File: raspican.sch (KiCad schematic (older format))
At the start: 3 parts, among them P1 CONN_13X2

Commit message: start wiring stuff up
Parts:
- added D1: LED, symbol LED
- added J2: CONN_01X06, symbol CONN_01X06
- added R10, R8, R9: 1KΩ, symbol R
- added R6: 18KΩ, symbol R
- added R7: 10KΩ, symbol R
- added SW1, SW2: BUTTON_FRAME, symbol BUTTON_FRAME
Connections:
- net +3.3V: now also R10.2, R9.2
- net +5V: now also J2.3 (P3)
- net GND: now also J2.1 (P1), J2.2 (P2), R6.2, R8.1, SW1.1, SW1.4, SW1.5, SW2.1, SW2.4, SW2.5
- net GPIO23: now also R9.1, SW2.2
- net GPIO24: now also R10.1, SW1.2
- net GPIO25: now also U?.13 (~INT)
- net GPIO7(CE1): now also D1.2 (A)
- net RXD: now also J2.4 (P4)
- net TXD: now also J2.5 (P5)
- net at U?.1 (TXCAN): now also U?.1 (TXD)
- net at U?.2 (RXCAN): now also R6.1, R7.2
- net at U?.4 (RXD): now also R7.1
- new net: D1.1 (K), R8.2
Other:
- moved on the sheet: P1, U?

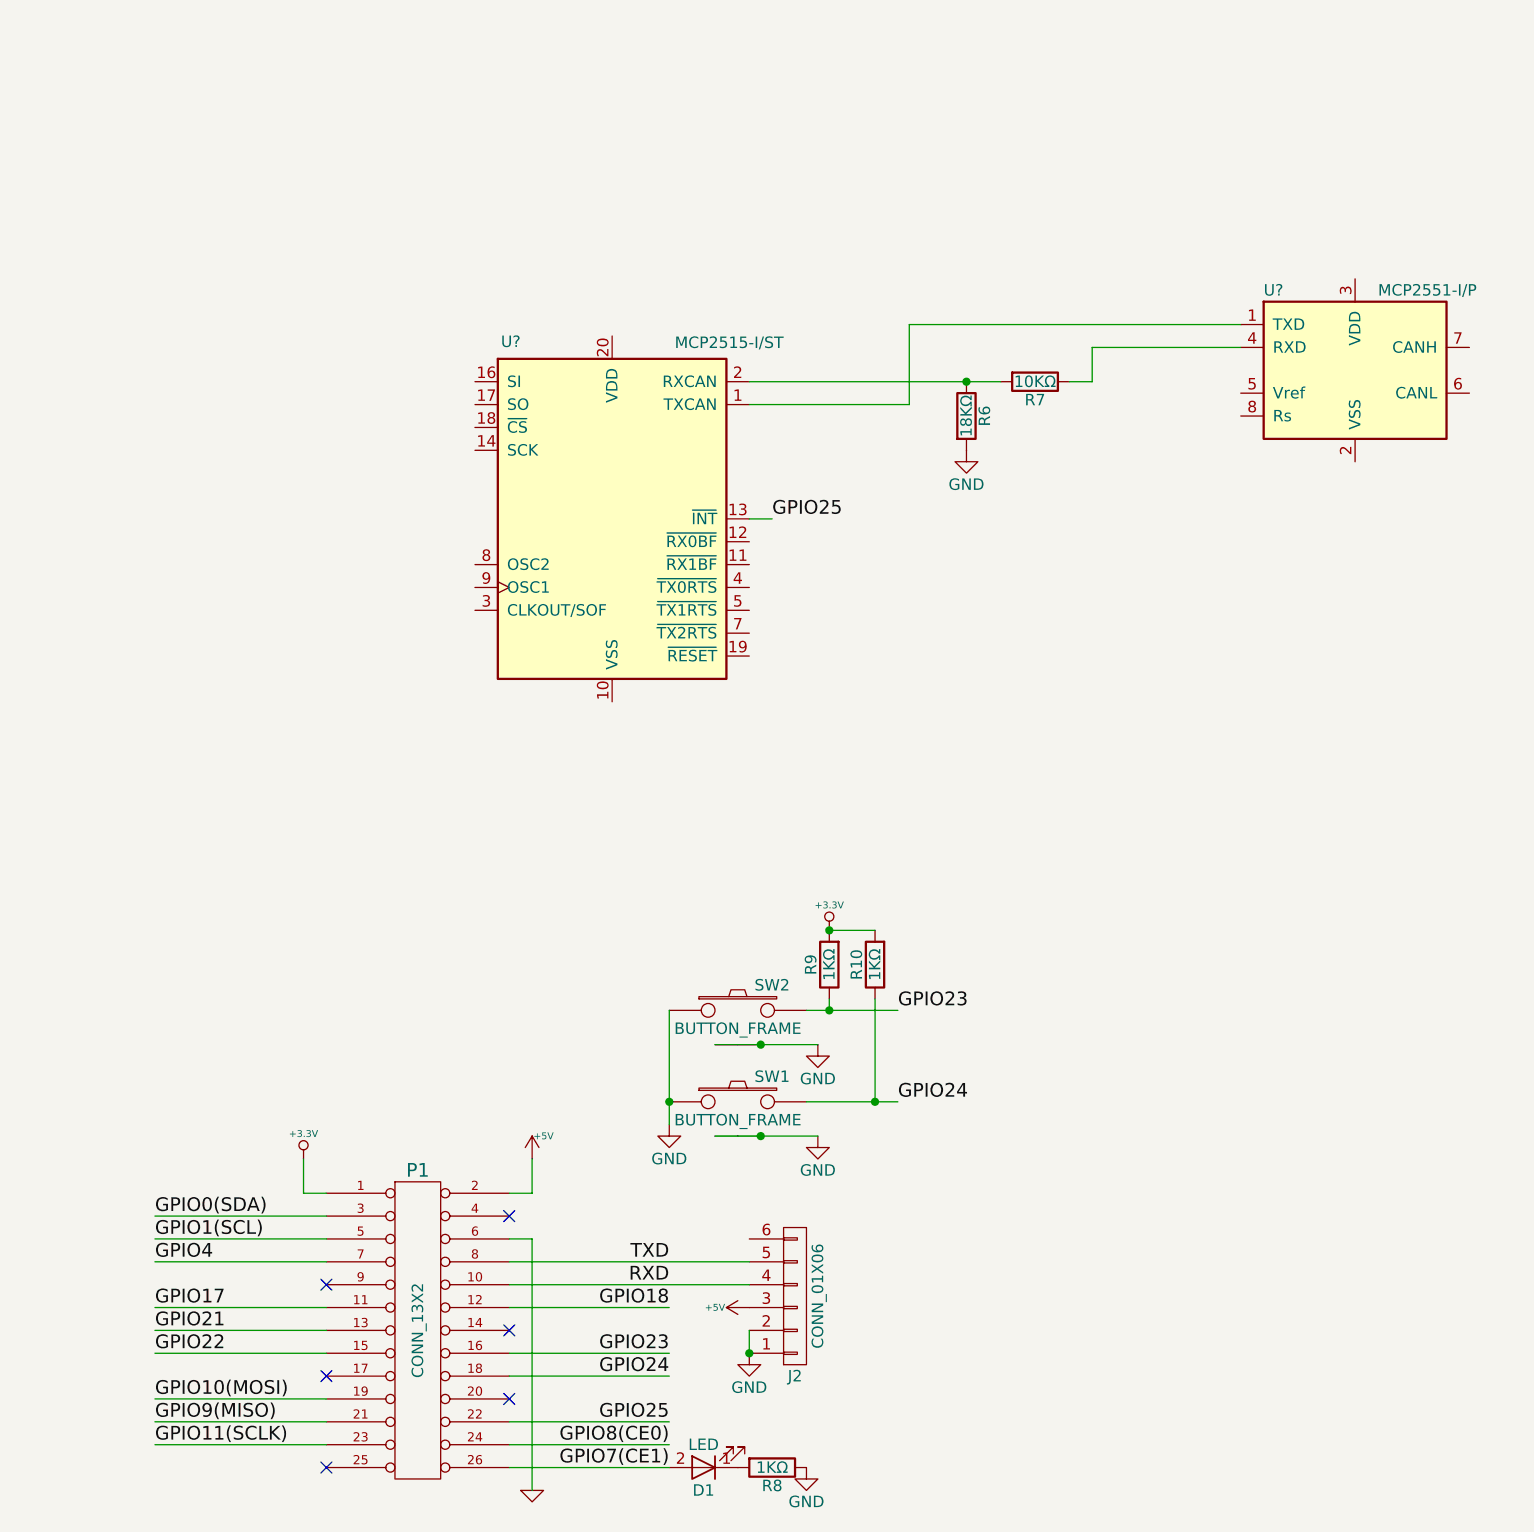
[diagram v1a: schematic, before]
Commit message: replace mcp2515 with correct DIP/SOIC pinout
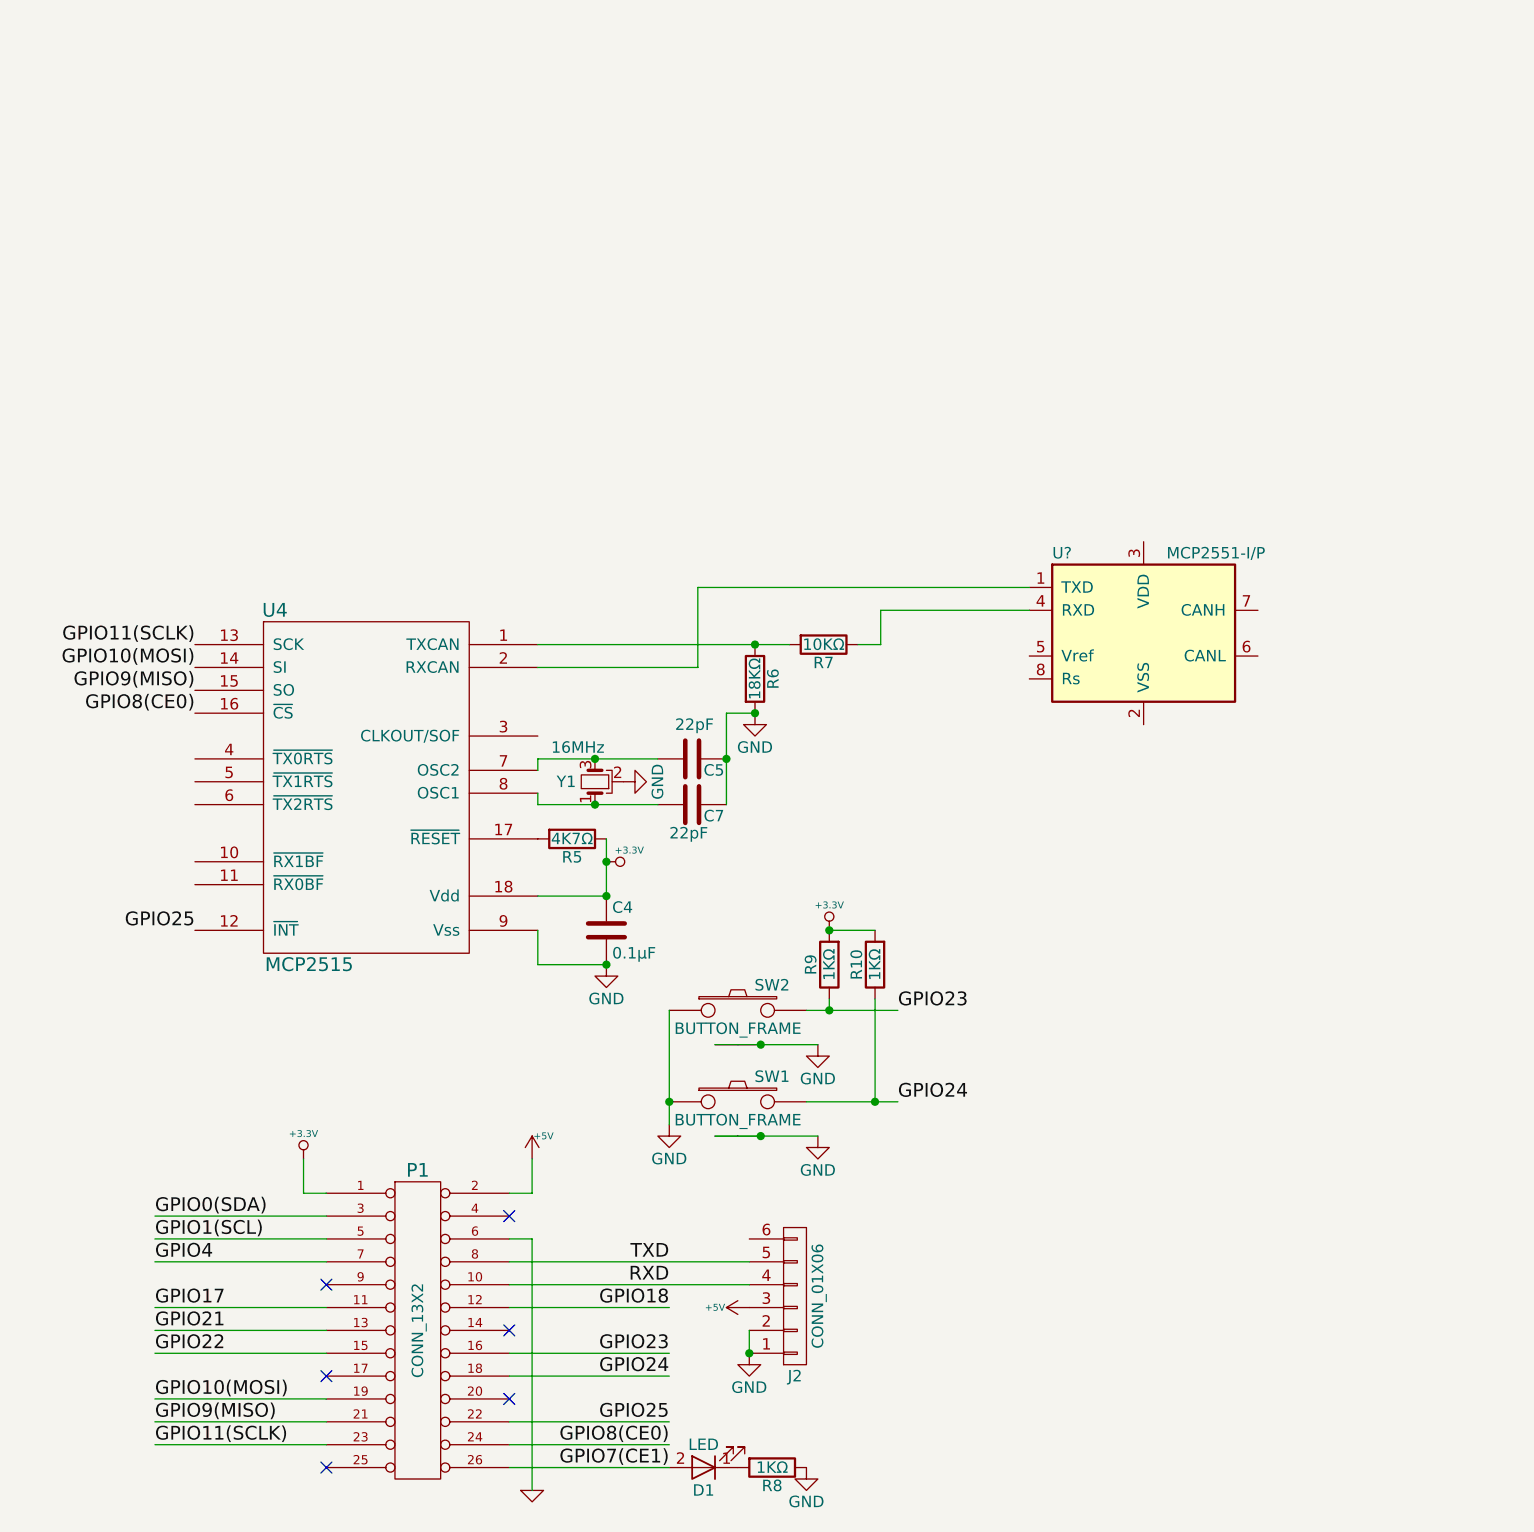
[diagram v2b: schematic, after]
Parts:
- removed U?: MCP2515-I/ST, Housings_SSOP:TSSOP-20_4.4x6.5mm_Pitch0.65mm, symbol MCP2515-I/ST
- added C4: 0.1μF, symbol C
- added C5, C7: 22pF, symbol C
- added R5: 4K7Ω, symbol R
- added U4: MCP2515, symbol MCP2515
- added Y1: 16MHz, symbol Crystal_GND2_Small
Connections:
- net +3.3V: now also C4.1, R5.1, U4.18 (Vdd)
- net GND: now also C4.2, C5.1, C7.1, U4.9 (Vss), Y1.2
- net GPIO10(MOSI): now also U4.14 (SI)
- net GPIO11(SCLK): now also U4.13 (SCK)
- net GPIO25: now also U4.12 (~INT)
- net GPIO8(CE0): now also U4.16 (~CS)
- net GPIO9(MISO): now also U4.15 (SO)
- net at U?.1 (TXD): now also U4.2 (RXCAN)
- net at R6.1, R7.2: now also U4.1 (TXCAN)
- new net: R5.2, U4.17 (~RESET)
- new net: C5.2, U4.7 (OSC2), Y1.3
- new net: C7.2, U4.8 (OSC1), Y1.1
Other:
- moved on the sheet: R6, R7, U?
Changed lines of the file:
@@
 LIBS:valves
 LIBS:arbduino-cache
+LIBS:eelib
 LIBS:raspican-cache
 EELAYER 25 0
@@
 GPIO7(CE1)
 $Comp
-L MCP2515-I/ST U?
-U 1 1 58B8BAFD
-P 3250 3100
-F 0 "U?" H 2850 3875 50  0000 R CNN
-F 1 "MCP2515-I/ST" H 4000 3900 50  0000 R TNN
-F 2 "Housings_SSOP:TSSOP-20_4.4x6.5mm_Pitch0.65mm" H 3250 2200 50  0001 C CIN
-F 3 "" H 3350 2300 50  0001 C CNN
-	1    3250 3100
-	1    0    0    -1
-$EndComp
-$Comp
 L MCP2551-I/P U?
 U 1 1 58B8BB6A
-P 6500 2450
-F 0 "U?" H 6100 2800 50  0000 L CNN
-F 1 "MCP2551-I/P" H 6600 2800 50  0000 L CNN
-F 2 "Housings_DIP:DIP-8_W7.62mm" H 6500 1950 50  0001 C CIN
-F 3 "" H 6500 2450 50  0001 C CNN
-	1    6500 2450
+P 5575 3600
+F 0 "U?" H 5175 3950 50  0000 L CNN
+F 1 "MCP2551-I/P" H 5675 3950 50  0000 L CNN
+F 2 "Housings_DIP:DIP-8_W7.62mm" H 5575 3100 50  0001 C CIN
+F 3 "" H 5575 3600 50  0001 C CNN
+	1    5575 3600
 	1    0    0    -1
 $EndComp
@@
 	3700 5400 4150 5400
 Connection ~ 3900 5400
-Text Label 3950 3100 0    60   ~ 0
+Text Label 1425 4900 2    60   ~ 0
 GPIO25
 Wire Wire Line
-	3950 3100 3850 3100
-Wire Wire Line
-	3850 2600 4550 2600
-Wire Wire Line
-	4550 2600 4550 2250
-Wire Wire Line
-	4550 2250 6000 2250
+	2925 3750 3625 3750
+Wire Wire Line
+	3625 3750 3625 3400
+Wire Wire Line
+	3625 3400 5075 3400
 $Comp
 L R R7
 U 1 1 58B9F632
-P 5100 2500
-F 0 "R7" V 5180 2500 50  0000 C CNN
-F 1 "10KΩ" V 5100 2500 50  0000 C CNN
-F 2 "" V 5030 2500 50  0001 C CNN
-F 3 "" H 5100 2500 50  0001 C CNN
-	1    5100 2500
+P 4175 3650
+F 0 "R7" V 4255 3650 50  0000 C CNN
+F 1 "10KΩ" V 4175 3650 50  0000 C CNN
+F 2 "" V 4105 3650 50  0001 C CNN
+F 3 "" H 4175 3650 50  0001 C CNN
+	1    4175 3650
 	0    1    1    0
 $EndComp
 Wire Wire Line
-	3850 2500 4950 2500
-Wire Wire Line
-	5250 2500 5350 2500
-Wire Wire Line
-	5350 2500 5350 2350
-Wire Wire Line
-	5350 2350 6000 2350
+	2925 3650 4025 3650
+Wire Wire Line
+	4325 3650 4425 3650
+Wire Wire Line
+	4425 3650 4425 3500
+Wire Wire Line
+	4425 3500 5075 3500
 $Comp
 L R R6
 U 1 1 58B9F818
-P 4800 2650
-F 0 "R6" V 4880 2650 50  0000 C CNN
-F 1 "18KΩ" V 4800 2650 50  0000 C CNN
-F 2 "" V 4730 2650 50  0001 C CNN
-F 3 "" H 4800 2650 50  0001 C CNN
-	1    4800 2650
-	1    0    0    -1
-$EndComp
-Connection ~ 4800 2500
+P 3875 3800
+F 0 "R6" V 3955 3800 50  0000 C CNN
+F 1 "18KΩ" V 3875 3800 50  0000 C CNN
+F 2 "" V 3805 3800 50  0001 C CNN
+F 3 "" H 3875 3800 50  0001 C CNN
+	1    3875 3800
+	1    0    0    -1
+$EndComp
+Connection ~ 3875 3650
 $Comp
 L GND #PWR?
 U 1 1 58B9F8A3
-P 4800 2800
-F 0 "#PWR?" H 4800 2550 50  0001 C CNN
-F 1 "GND" H 4800 2650 50  0000 C CNN
-F 2 "" H 4800 2800 50  0001 C CNN
-F 3 "" H 4800 2800 50  0001 C CNN
-	1    4800 2800
-	1    0    0    -1
-$EndComp
+P 3875 3950
+F 0 "#PWR?" H 3875 3700 50  0001 C CNN
+F 1 "GND" H 3875 3800 50  0000 C CNN
+F 2 "" H 3875 3950 50  0001 C CNN
+F 3 "" H 3875 3950 50  0001 C CNN
+	1    3875 3950
+	1    0    0    -1
+$EndComp
+$Comp
+L R R5
+U 1 1 58B9F9D1
+P 3075 4500
+F 0 "R5" V 3155 4500 50  0000 C CNN
+F 1 "4K7Ω" V 3075 4500 50  0000 C CNN
+F 2 "" V 3005 4500 50  0001 C CNN
+F 3 "" H 3075 4500 50  0001 C CNN
+	1    3075 4500
+	0    1    1    0
+$EndComp
+$Comp
+L +3.3V-RESCUE-raspican #PWR?
+U 1 1 58B9FB76
+P 3225 4600
+F 0 "#PWR?" H 3225 4560 30  0001 C CNN
+F 1 "+3.3V" V 3175 4700 30  0000 C CNN
+F 2 "" H 3225 4600 60  0001 C CNN
+F 3 "" H 3225 4600 60  0001 C CNN
+	1    3225 4600
+	0    1    1    0
+$EndComp
+$Comp
+L MCP2515 U4
+U 1 1 58B9FCF9
+P 2175 4300
+F 0 "U4" H 1775 5100 60  0000 C CNN
+F 1 "MCP2515" H 1925 3550 60  0000 C CNN
+F 2 "" H 2175 4300 60  0001 C CNN
+F 3 "" H 2175 4300 60  0001 C CNN
+	1    2175 4300
+	1    0    0    -1
+$EndComp
+Wire Wire Line
+	3225 4500 3225 4750
+Wire Wire Line
+	3225 4750 2925 4750
+Connection ~ 3225 4600
+$Comp
+L C C4
+U 1 1 58BA000F
+P 3225 4900
+F 0 "C4" H 3250 5000 50  0000 L CNN
+F 1 "0.1μF" H 3250 4800 50  0000 L CNN
+F 2 "" H 3263 4750 50  0001 C CNN
+F 3 "" H 3225 4900 50  0001 C CNN
+	1    3225 4900
+	1    0    0    -1
+$EndComp
+Connection ~ 3225 4750
+$Comp
+L GND #PWR?
+U 1 1 58BA00B4
+P 3225 5050
+F 0 "#PWR?" H 3225 4800 50  0001 C CNN
+F 1 "GND" H 3225 4900 50  0000 C CNN
+F 2 "" H 3225 5050 50  0001 C CNN
+F 3 "" H 3225 5050 50  0001 C CNN
+	1    3225 5050
+	1    0    0    -1
+$EndComp
+Wire Wire Line
+	3225 5050 2925 5050
+Wire Wire Line
+	2925 5050 2925 4900
+Connection ~ 3225 5050
+$Comp
+L Crystal_GND2_Small Y1
+U 1 1 58BA01F9
+P 3175 4250
+F 0 "Y1" V 3175 4375 50  0000 C CNN
+F 1 "16MHz" V 3325 4325 50  0000 C CNN
+F 2 "" H 3175 4250 50  0001 C CNN
+F 3 "" H 3175 4250 50  0001 C CNN
+	1    3175 4250
+	0    -1   -1   0
+$EndComp
+Wire Wire Line
+	2925 4150 3450 4150
+Wire Wire Line
+	2925 4150 2925 4200
+Wire Wire Line
+	2925 4300 2925 4350
+Wire Wire Line
+	2925 4350 3450 4350
+$Comp
+L GND #PWR?
+U 1 1 58BA0360
+P 3300 4250
+F 0 "#PWR?" H 3300 4000 50  0001 C CNN
+F 1 "GND" H 3300 4100 50  0000 C CNN
+F 2 "" H 3300 4250 50  0001 C CNN
+F 3 "" H 3300 4250 50  0001 C CNN
+	1    3300 4250
+	0    -1   -1   0
+$EndComp
+$Comp
+L C C5
+U 1 1 58BA0567
+P 3600 4150
+F 0 "C5" V 3650 4200 50  0000 L CNN
+F 1 "22pF" V 3450 4075 50  0000 L CNN
+F 2 "" H 3638 4000 50  0001 C CNN
+F 3 "" H 3600 4150 50  0001 C CNN
+	1    3600 4150
+	0    1    1    0
+$EndComp
+$Comp
+L C C7
+U 1 1 58BA05DB
+P 3600 4350
+F 0 "C7" V 3650 4400 50  0000 L CNN
+F 1 "22pF" V 3725 4250 50  0000 L CNN
+F 2 "" H 3638 4200 50  0001 C CNN
+F 3 "" H 3600 4350 50  0001 C CNN
+	1    3600 4350
+	0    1    1    0
+$EndComp
+Wire Wire Line
+	3750 3950 3750 4350
+Wire Wire Line
+	3750 3950 3875 3950
+Connection ~ 3750 4150
+Connection ~ 3875 3950
+Connection ~ 3175 4150
+Connection ~ 3175 4350
+Text Label 1425 3950 2    60   ~ 0
+GPIO8(CE0)
+Text Label 1425 3750 2    60   ~ 0
+GPIO10(MOSI)
+Text Label 1425 3850 2    60   ~ 0
+GPIO9(MISO)
+Text Label 1425 3650 2    60   ~ 0
+GPIO11(SCLK)
 $EndSCHEMATC
